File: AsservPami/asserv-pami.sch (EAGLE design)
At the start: 31 parts, among them IC1 NUCLEO-G431KB, IC2 7805TV

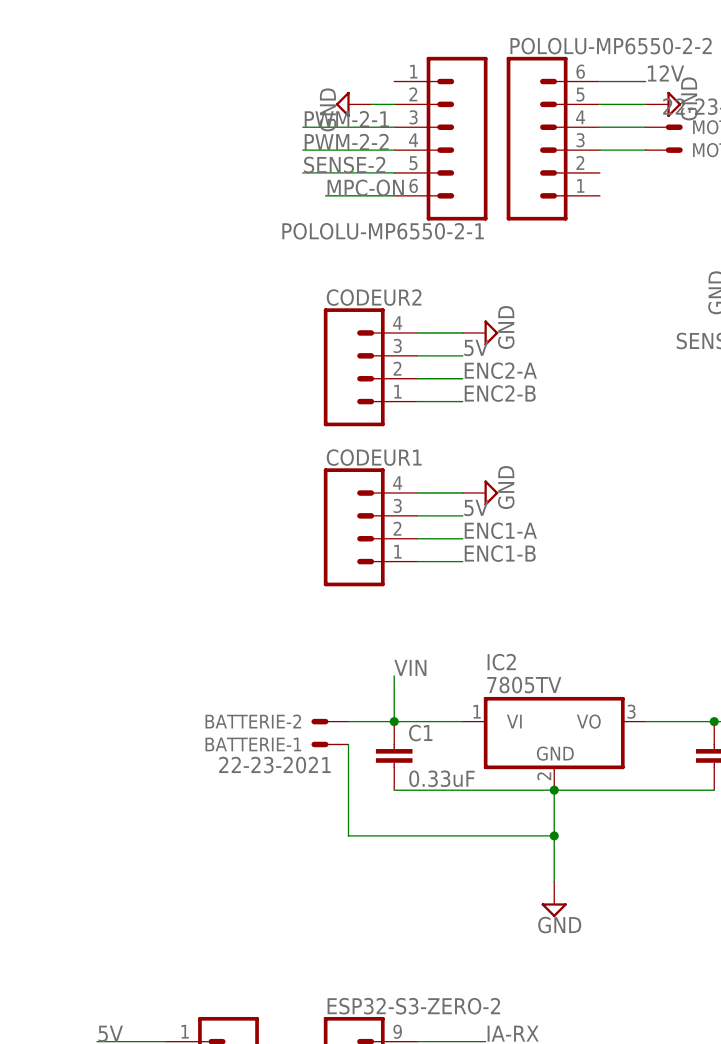
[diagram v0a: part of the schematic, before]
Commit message: ajout BAU et Voltmetre + label
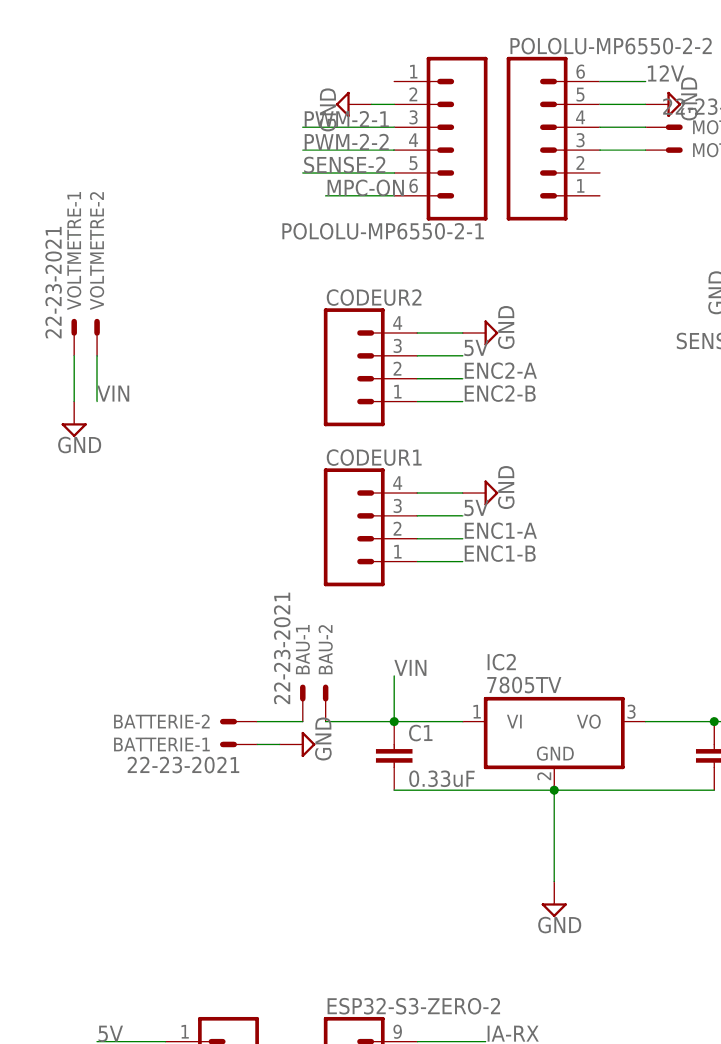
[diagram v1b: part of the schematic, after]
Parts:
- added BAU, VOLTMETRE: 22-23-2021, con-molex:22-23-2021
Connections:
- new net N$7: BATTERIE-2.S, BAU-1.S
- net GND: now also VOLTMETRE-1.S
- net VIN: now also BAU-2.S, VOLTMETRE-2.S; no longer BATTERIE-2.S
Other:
- moved on the sheet: BATTERIE-1, BATTERIE-2
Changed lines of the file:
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@@
 <part name="SUPPLY20" library="supply2" library_urn="urn:adsk.eagle:library:372" deviceset="GND" device=""/>
 <part name="C3" library="capacitor-wima" library_urn="urn:adsk.eagle:library:116" deviceset="C" device="5/2.5" value="0.33uF"/>
+<part name="SUPPLY21" library="supply2" library_urn="urn:adsk.eagle:library:372" deviceset="GND" device=""/>
+<part name="BAU" library="con-molex" library_urn="urn:adsk.eagle:library:165" deviceset="22-23-2021" device=""/>
+<part name="VOLTMETRE" library="con-molex" library_urn="urn:adsk.eagle:library:165" deviceset="22-23-2021" device=""/>
+<part name="SUPPLY22" library="supply2" library_urn="urn:adsk.eagle:library:372" deviceset="GND" device=""/>
 </parts>
 <sheets>
@@
 <attribute name="VALUE" x="63.5" y="120.015" size="1.778" layer="96"/>
 </instance>
-<instance part="BATTERIE" gate="-1" x="45.72" y="114.3" smashed="yes" rot="R180">
-<attribute name="NAME" x="43.18" y="115.062" size="1.524" layer="95" rot="R180"/>
-<attribute name="VALUE" x="46.482" y="112.903" size="1.778" layer="96" rot="R180"/>
-</instance>
-<instance part="BATTERIE" gate="-2" x="45.72" y="116.84" smashed="yes" rot="R180">
-<attribute name="NAME" x="43.18" y="117.602" size="1.524" layer="95" rot="R180"/>
+<instance part="BATTERIE" gate="-1" x="35.56" y="114.3" smashed="yes" rot="R180">
+<attribute name="NAME" x="33.02" y="115.062" size="1.524" layer="95" rot="R180"/>
+<attribute name="VALUE" x="36.322" y="112.903" size="1.778" layer="96" rot="R180"/>
+</instance>
+<instance part="BATTERIE" gate="-2" x="35.56" y="116.84" smashed="yes" rot="R180">
+<attribute name="NAME" x="33.02" y="117.602" size="1.524" layer="95" rot="R180"/>
 </instance>
 <instance part="C1" gate="G$1" x="53.34" y="114.3" smashed="yes">
@@
 <attribute name="NAME" x="126.619" y="105.664" size="1.778" layer="95" rot="R90"/>
 <attribute name="VALUE" x="131.699" y="105.664" size="1.778" layer="96" rot="R90"/>
+</instance>
+<instance part="SUPPLY21" gate="GND" x="43.18" y="114.3" smashed="yes" rot="R90">
+<attribute name="VALUE" x="46.355" y="112.395" size="1.778" layer="96" rot="R90"/>
+</instance>
+<instance part="BAU" gate="-1" x="43.18" y="119.38" smashed="yes" rot="R90">
+<attribute name="NAME" x="43.942" y="121.92" size="1.524" layer="95" rot="R90"/>
+<attribute name="VALUE" x="41.783" y="118.618" size="1.778" layer="96" rot="R90"/>
+</instance>
+<instance part="BAU" gate="-2" x="45.72" y="119.38" smashed="yes" rot="R90">
+<attribute name="NAME" x="46.482" y="121.92" size="1.524" layer="95" rot="R90"/>
+</instance>
+<instance part="VOLTMETRE" gate="-1" x="17.78" y="160.02" smashed="yes" rot="R90">
+<attribute name="NAME" x="18.542" y="162.56" size="1.524" layer="95" rot="R90"/>
+<attribute name="VALUE" x="16.383" y="159.258" size="1.778" layer="96" rot="R90"/>
+</instance>
+<instance part="VOLTMETRE" gate="-2" x="20.32" y="160.02" smashed="yes" rot="R90">
+<attribute name="NAME" x="21.082" y="162.56" size="1.524" layer="95" rot="R90"/>
+</instance>
+<instance part="SUPPLY22" gate="GND" x="17.78" y="149.86" smashed="yes">
+<attribute name="VALUE" x="15.875" y="146.685" size="1.778" layer="96"/>
 </instance>
 </instances>
@@
 <wire x1="71.12" y1="109.22" x2="88.9" y2="109.22" width="0.1524" layer="91"/>
 <junction x="71.12" y="109.22"/>
-<pinref part="BATTERIE" gate="-1" pin="S"/>
-<wire x1="48.26" y1="114.3" x2="48.26" y2="104.14" width="0.1524" layer="91"/>
-<wire x1="48.26" y1="104.14" x2="71.12" y2="104.14" width="0.1524" layer="91"/>
-<wire x1="71.12" y1="104.14" x2="71.12" y2="109.22" width="0.1524" layer="91"/>
-<junction x="71.12" y="104.14"/>
 <pinref part="SUPPLY9" gate="GND" pin="GND"/>
-<wire x1="71.12" y1="104.14" x2="71.12" y2="99.06" width="0.1524" layer="91"/>
+<wire x1="71.12" y1="109.22" x2="71.12" y2="99.06" width="0.1524" layer="91"/>
 </segment>
 <segment>
@@
 <pinref part="SERVO1" gate="J1" pin="3"/>
 </segment>
+<segment>
+<pinref part="SUPPLY21" gate="GND" pin="GND"/>
+<wire x1="38.1" y1="114.3" x2="40.64" y2="114.3" width="0.1524" layer="91"/>
+<pinref part="BATTERIE" gate="-1" pin="S"/>
+</segment>
+<segment>
+<pinref part="SUPPLY22" gate="GND" pin="GND"/>
+<wire x1="17.78" y1="157.48" x2="17.78" y2="152.4" width="0.1524" layer="91"/>
+<pinref part="VOLTMETRE" gate="-1" pin="S"/>
+</segment>
 </net>
 <net name="N$1" class="0">
@@
 <net name="VIN" class="0">
 <segment>
-<pinref part="BATTERIE" gate="-2" pin="S"/>
 <pinref part="C1" gate="G$1" pin="1"/>
-<wire x1="48.26" y1="116.84" x2="53.34" y2="116.84" width="0.1524" layer="91"/>
 <pinref part="IC2" gate="A1" pin="VI"/>
 <wire x1="53.34" y1="116.84" x2="60.96" y2="116.84" width="0.1524" layer="91"/>
@@
 <wire x1="53.34" y1="116.84" x2="53.34" y2="121.92" width="0.1524" layer="91"/>
 <label x="53.34" y="121.92" size="1.778" layer="95"/>
+<pinref part="BAU" gate="-2" pin="S"/>
+<wire x1="45.72" y1="116.84" x2="53.34" y2="116.84" width="0.1524" layer="91"/>
 </segment>
 <segment>
@@
 <label x="132.08" y="101.6" size="1.778" layer="95"/>
 </segment>
+<segment>
+<pinref part="VOLTMETRE" gate="-2" pin="S"/>
+<wire x1="20.32" y1="157.48" x2="20.32" y2="152.4" width="0.1524" layer="91"/>
+<label x="20.32" y="152.4" size="1.778" layer="95"/>
+</segment>
 </net>
 <net name="SDA" class="0">
@@
 </segment>
 </net>
+<net name="N$7" class="0">
+<segment>
+<pinref part="BATTERIE" gate="-2" pin="S"/>
+<pinref part="BAU" gate="-1" pin="S"/>
+<wire x1="38.1" y1="116.84" x2="43.18" y2="116.84" width="0.1524" layer="91"/>
+</segment>
+</net>

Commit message: fix i2c
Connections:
- net SCL: now also ESP32-S3-ZERO-2.2; no longer ESP32-S3-ZERO-2.6
- net SDA: now also ESP32-S3-ZERO-2.3; no longer ESP32-S3-ZERO-2.7
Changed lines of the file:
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@@
 <net name="SDA" class="0">
-<segment>
-<pinref part="ESP32-S3-ZERO-2" gate="J1" pin="7"/>
-<wire x1="55.88" y1="76.2" x2="63.5" y2="76.2" width="0.1524" layer="91"/>
-<label x="63.5" y="76.2" size="1.778" layer="95"/>
-</segment>
 <segment>
 <pinref part="I2C" gate="J1" pin="1"/>
@@
 <label x="96.52" y="68.58" size="1.778" layer="95" rot="R90"/>
 </segment>
+<segment>
+<wire x1="55.88" y1="66.04" x2="63.5" y2="66.04" width="0.1524" layer="91"/>
+<label x="63.5" y="66.04" size="1.778" layer="95"/>
+<pinref part="ESP32-S3-ZERO-2" gate="J1" pin="3"/>
+</segment>
 </net>
 <net name="SCL" class="0">
-<segment>
-<pinref part="ESP32-S3-ZERO-2" gate="J1" pin="6"/>
-<wire x1="55.88" y1="73.66" x2="63.5" y2="73.66" width="0.1524" layer="91"/>
-<label x="63.5" y="73.66" size="1.778" layer="95"/>
-</segment>
 <segment>
 <pinref part="I2C" gate="J1" pin="2"/>
@@
 <label x="99.06" y="68.58" size="1.778" layer="95" rot="R90"/>
 </segment>
+<segment>
+<wire x1="55.88" y1="63.5" x2="63.5" y2="63.5" width="0.1524" layer="91"/>
+<label x="63.5" y="63.5" size="1.778" layer="95"/>
+<pinref part="ESP32-S3-ZERO-2" gate="J1" pin="2"/>
+</segment>
 </net>

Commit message: fix name
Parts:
- renumbered ESP32-S3-ZERO-1 to ESP32-C3-ZERO-1, ESP32-S3-ZERO-2 to ESP32-C3-ZERO-2
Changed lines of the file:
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@@
 <part name="POLOLU-U3V40F12" library="SparkFun-Connectors" library_urn="urn:adsk.eagle:library:513" deviceset="CONN_06" device="NO_SILK_FEMALE_PTH" package3d_urn="urn:adsk.eagle:package:38130/2"/>
 <part name="SUPPLY10" library="supply2" library_urn="urn:adsk.eagle:library:372" deviceset="GND" device=""/>
-<part name="ESP32-S3-ZERO-2" library="SparkFun-Connectors" library_urn="urn:adsk.eagle:library:513" deviceset="CONN_09" device="LONGPADS" package3d_urn="urn:adsk.eagle:package:38155/2"/>
-<part name="ESP32-S3-ZERO-1" library="SparkFun-Connectors" library_urn="urn:adsk.eagle:library:513" deviceset="CONN_09" device="LONGPADS" package3d_urn="urn:adsk.eagle:package:38155/2"/>
+<part name="ESP32-C3-ZERO-2" library="SparkFun-Connectors" library_urn="urn:adsk.eagle:library:513" deviceset="CONN_09" device="LONGPADS" package3d_urn="urn:adsk.eagle:package:38155/2"/>
+<part name="ESP32-C3-ZERO-1" library="SparkFun-Connectors" library_urn="urn:adsk.eagle:library:513" deviceset="CONN_09" device="LONGPADS" package3d_urn="urn:adsk.eagle:package:38155/2"/>
 <part name="SUPPLY13" library="supply2" library_urn="urn:adsk.eagle:library:372" deviceset="GND" device=""/>
 <part name="I2C" library="SparkFun-Connectors" library_urn="urn:adsk.eagle:library:513" deviceset="CONN_04" device="PTH" package3d_urn="urn:adsk.eagle:package:38085/2"/>
@@
 <attribute name="VALUE" x="122.555" y="98.425" size="1.778" layer="96"/>
 </instance>
-<instance part="ESP32-S3-ZERO-2" gate="J1" x="45.72" y="71.12" smashed="yes">
+<instance part="ESP32-C3-ZERO-2" gate="J1" x="45.72" y="71.12" smashed="yes">
 <attribute name="VALUE" x="45.72" y="56.134" size="1.778" layer="96" font="vector"/>
 <attribute name="NAME" x="45.72" y="84.328" size="1.778" layer="95" font="vector"/>
 </instance>
-<instance part="ESP32-S3-ZERO-1" gate="J1" x="38.1" y="71.12" smashed="yes" rot="R180">
+<instance part="ESP32-C3-ZERO-1" gate="J1" x="38.1" y="71.12" smashed="yes" rot="R180">
 <attribute name="VALUE" x="38.1" y="86.106" size="1.778" layer="96" font="vector" rot="R180"/>
 <attribute name="NAME" x="38.1" y="57.912" size="1.778" layer="95" font="vector" rot="R180"/>
@@
 </segment>
 <segment>
-<pinref part="ESP32-S3-ZERO-1" gate="J1" pin="2"/>
+<pinref part="ESP32-C3-ZERO-1" gate="J1" pin="2"/>
 <pinref part="SUPPLY13" gate="GND" pin="GND"/>
 <wire x1="27.94" y1="78.74" x2="20.32" y2="78.74" width="0.1524" layer="91"/>
@@
 </segment>
 <segment>
-<pinref part="ESP32-S3-ZERO-2" gate="J1" pin="8"/>
+<pinref part="ESP32-C3-ZERO-2" gate="J1" pin="8"/>
 <wire x1="55.88" y1="78.74" x2="63.5" y2="78.74" width="0.1524" layer="91"/>
 <label x="63.5" y="78.74" size="1.778" layer="95"/>
@@
 </segment>
 <segment>
-<pinref part="ESP32-S3-ZERO-2" gate="J1" pin="9"/>
+<pinref part="ESP32-C3-ZERO-2" gate="J1" pin="9"/>
 <wire x1="55.88" y1="81.28" x2="63.5" y2="81.28" width="0.1524" layer="91"/>
 <label x="63.5" y="81.28" size="1.778" layer="95"/>
@@
 </segment>
 <segment>
-<pinref part="ESP32-S3-ZERO-1" gate="J1" pin="1"/>
+<pinref part="ESP32-C3-ZERO-1" gate="J1" pin="1"/>
 <wire x1="27.94" y1="81.28" x2="20.32" y2="81.28" width="0.1524" layer="91"/>
 <label x="20.32" y="81.28" size="1.778" layer="95"/>
@@
 <wire x1="55.88" y1="66.04" x2="63.5" y2="66.04" width="0.1524" layer="91"/>
 <label x="63.5" y="66.04" size="1.778" layer="95"/>
-<pinref part="ESP32-S3-ZERO-2" gate="J1" pin="3"/>
+<pinref part="ESP32-C3-ZERO-2" gate="J1" pin="3"/>
 </segment>
 </net>
@@
 <wire x1="55.88" y1="63.5" x2="63.5" y2="63.5" width="0.1524" layer="91"/>
 <label x="63.5" y="63.5" size="1.778" layer="95"/>
-<pinref part="ESP32-S3-ZERO-2" gate="J1" pin="2"/>
+<pinref part="ESP32-C3-ZERO-2" gate="J1" pin="2"/>
 </segment>
 </net>
@@
 <wire x1="27.94" y1="73.66" x2="17.78" y2="73.66" width="0.1524" layer="91"/>
 <label x="17.78" y="73.66" size="1.778" layer="95"/>
-<pinref part="ESP32-S3-ZERO-1" gate="J1" pin="4"/>
+<pinref part="ESP32-C3-ZERO-1" gate="J1" pin="4"/>
 </segment>
 </net>
@@
 <wire x1="27.94" y1="71.12" x2="17.78" y2="71.12" width="0.1524" layer="91"/>
 <label x="17.78" y="71.12" size="1.778" layer="95"/>
-<pinref part="ESP32-S3-ZERO-1" gate="J1" pin="5"/>
+<pinref part="ESP32-C3-ZERO-1" gate="J1" pin="5"/>
 </segment>
 </net>
@@
 <wire x1="27.94" y1="68.58" x2="17.78" y2="68.58" width="0.1524" layer="91"/>
 <label x="17.78" y="68.58" size="1.778" layer="95"/>
-<pinref part="ESP32-S3-ZERO-1" gate="J1" pin="6"/>
+<pinref part="ESP32-C3-ZERO-1" gate="J1" pin="6"/>
 </segment>
 </net>
@@
 <wire x1="27.94" y1="66.04" x2="17.78" y2="66.04" width="0.1524" layer="91"/>
 <label x="17.78" y="66.04" size="1.778" layer="95"/>
-<pinref part="ESP32-S3-ZERO-1" gate="J1" pin="7"/>
+<pinref part="ESP32-C3-ZERO-1" gate="J1" pin="7"/>
 </segment>
 </net>
@@
 <wire x1="27.94" y1="63.5" x2="17.78" y2="63.5" width="0.1524" layer="91"/>
 <label x="17.78" y="63.5" size="1.778" layer="95"/>
-<pinref part="ESP32-S3-ZERO-1" gate="J1" pin="8"/>
+<pinref part="ESP32-C3-ZERO-1" gate="J1" pin="8"/>
 </segment>
 </net>
@@
 <wire x1="27.94" y1="60.96" x2="17.78" y2="60.96" width="0.1524" layer="91"/>
 <label x="17.78" y="60.96" size="1.778" layer="95"/>
-<pinref part="ESP32-S3-ZERO-1" gate="J1" pin="9"/>
+<pinref part="ESP32-C3-ZERO-1" gate="J1" pin="9"/>
 </segment>
 </net>
@@
 <pinref part="UART" gate="-1" pin="S"/>
 <wire x1="68.58" y1="66.04" x2="68.58" y2="68.58" width="0.1524" layer="91"/>
-<pinref part="ESP32-S3-ZERO-2" gate="J1" pin="4"/>
+<pinref part="ESP32-C3-ZERO-2" gate="J1" pin="4"/>
 <wire x1="68.58" y1="68.58" x2="55.88" y2="68.58" width="0.1524" layer="91"/>
 </segment>
@@
 <pinref part="UART" gate="-2" pin="S"/>
 <wire x1="66.04" y1="66.04" x2="66.04" y2="71.12" width="0.1524" layer="91"/>
-<pinref part="ESP32-S3-ZERO-2" gate="J1" pin="5"/>
+<pinref part="ESP32-C3-ZERO-2" gate="J1" pin="5"/>
 <wire x1="66.04" y1="71.12" x2="55.88" y2="71.12" width="0.1524" layer="91"/>
 </segment>

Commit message: fix pami woard
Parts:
- added R-5K5, R-5K6: (no value), rcl:R-EU_0204/7
- C1: value 0.33uF -> 0.1uF
- C2: value 0.1uF -> 22uF
- C3: value 0.33uF -> 33uF
- IC2: value 7805TV -> L4941BV
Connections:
- net 5V: now also R-5K5.2, R-5K6.2; no longer IC1.+5V
- net SCL: now also R-5K6.1
- net SDA: now also R-5K5.1
- net VIN: now also IC1.VIN
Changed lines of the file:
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@@
 <part name="USB-DEBUG" library="SparkFun-Connectors" library_urn="urn:adsk.eagle:library:513" deviceset="CONN_05" device="NO_SILK" package3d_urn="urn:adsk.eagle:package:38108/2"/>
 <part name="SUPPLY8" library="supply2" library_urn="urn:adsk.eagle:library:372" deviceset="GND" device=""/>
-<part name="IC2" library="linear" library_urn="urn:adsk.eagle:library:262" deviceset="78*" device="TV" technology="05"/>
+<part name="IC2" library="linear" library_urn="urn:adsk.eagle:library:262" deviceset="78*" device="TV" technology="05" value="L4941BV"/>
 <part name="BATTERIE" library="con-molex" library_urn="urn:adsk.eagle:library:165" deviceset="22-23-2021" device=""/>
-<part name="C1" library="capacitor-wima" library_urn="urn:adsk.eagle:library:116" deviceset="C" device="5/2.5" value="0.33uF"/>
-<part name="C2" library="capacitor-wima" library_urn="urn:adsk.eagle:library:116" deviceset="C" device="5/2.5" value="0.1uF"/>
+<part name="C1" library="capacitor-wima" library_urn="urn:adsk.eagle:library:116" deviceset="C" device="5/2.5" value="0.1uF"/>
+<part name="C2" library="capacitor-wima" library_urn="urn:adsk.eagle:library:116" deviceset="C" device="5/2.5" value="22uF"/>
 <part name="SUPPLY9" library="supply2" library_urn="urn:adsk.eagle:library:372" deviceset="GND" device=""/>
 <part name="FRAME1" library="frames" library_urn="urn:adsk.eagle:library:229" deviceset="A4-SMALL-DOCFIELD" device=""/>
@@
 <part name="SUPPLY19" library="supply2" library_urn="urn:adsk.eagle:library:372" deviceset="GND" device=""/>
 <part name="SUPPLY20" library="supply2" library_urn="urn:adsk.eagle:library:372" deviceset="GND" device=""/>
-<part name="C3" library="capacitor-wima" library_urn="urn:adsk.eagle:library:116" deviceset="C" device="5/2.5" value="0.33uF"/>
+<part name="C3" library="capacitor-wima" library_urn="urn:adsk.eagle:library:116" deviceset="C" device="5/2.5" value="33uF"/>
 <part name="SUPPLY21" library="supply2" library_urn="urn:adsk.eagle:library:372" deviceset="GND" device=""/>
 <part name="BAU" library="con-molex" library_urn="urn:adsk.eagle:library:165" deviceset="22-23-2021" device=""/>
 <part name="VOLTMETRE" library="con-molex" library_urn="urn:adsk.eagle:library:165" deviceset="22-23-2021" device=""/>
 <part name="SUPPLY22" library="supply2" library_urn="urn:adsk.eagle:library:372" deviceset="GND" device=""/>
+<part name="R-5K5" library="rcl" library_urn="urn:adsk.eagle:library:334" deviceset="R-EU_" device="0204/7" package3d_urn="urn:adsk.eagle:package:23498/1"/>
+<part name="R-5K6" library="rcl" library_urn="urn:adsk.eagle:library:334" deviceset="R-EU_" device="0204/7" package3d_urn="urn:adsk.eagle:package:23498/1"/>
 </parts>
 <sheets>
@@
 <attribute name="VALUE" x="15.875" y="146.685" size="1.778" layer="96"/>
 </instance>
+<instance part="R-5K5" gate="G$1" x="48.26" y="35.56" smashed="yes" rot="R270">
+<attribute name="NAME" x="49.7586" y="39.37" size="1.778" layer="95" rot="R270"/>
+<attribute name="VALUE" x="44.958" y="39.37" size="1.778" layer="96" rot="R270"/>
+</instance>
+<instance part="R-5K6" gate="G$1" x="53.34" y="35.56" smashed="yes" rot="R270">
+<attribute name="NAME" x="54.8386" y="39.37" size="1.778" layer="95" rot="R270"/>
+<attribute name="VALUE" x="50.038" y="39.37" size="1.778" layer="96" rot="R270"/>
+</instance>
 </instances>
 <busses>
@@
 <net name="5V" class="0">
 <segment>
-<pinref part="IC1" gate="G$1" pin="+5V"/>
-<wire x1="144.78" y1="165.1" x2="149.86" y2="165.1" width="0.1524" layer="91"/>
-<label x="149.86" y="165.1" size="1.778" layer="95"/>
-</segment>
-<segment>
 <pinref part="CODEUR2" gate="J1" pin="3"/>
 <wire x1="55.88" y1="157.48" x2="60.96" y2="157.48" width="0.1524" layer="91"/>
@@
 <label x="81.28" y="40.64" size="1.778" layer="95" rot="R270"/>
 <pinref part="SERVO1" gate="J1" pin="2"/>
+</segment>
+<segment>
+<pinref part="R-5K5" gate="G$1" pin="2"/>
+<wire x1="48.26" y1="30.48" x2="48.26" y2="22.86" width="0.1524" layer="91"/>
+<label x="48.26" y="22.86" size="1.778" layer="95" rot="R90"/>
+</segment>
+<segment>
+<pinref part="R-5K6" gate="G$1" pin="2"/>
+<wire x1="53.34" y1="30.48" x2="53.34" y2="22.86" width="0.1524" layer="91"/>
+<label x="53.34" y="22.86" size="1.778" layer="95" rot="R90"/>
 </segment>
 </net>
@@
 <label x="20.32" y="152.4" size="1.778" layer="95"/>
 </segment>
+<segment>
+<pinref part="IC1" gate="G$1" pin="VIN"/>
+<wire x1="144.78" y1="172.72" x2="149.86" y2="172.72" width="0.1524" layer="91"/>
+<label x="149.86" y="172.72" size="1.778" layer="95"/>
+</segment>
 </net>
 <net name="SDA" class="0">
@@
 <pinref part="ESP32-C3-ZERO-2" gate="J1" pin="3"/>
 </segment>
+<segment>
+<pinref part="R-5K5" gate="G$1" pin="1"/>
+<wire x1="48.26" y1="40.64" x2="48.26" y2="45.72" width="0.1524" layer="91"/>
+<label x="48.26" y="45.72" size="1.778" layer="95"/>
+</segment>
 </net>
 <net name="SCL" class="0">
@@
 <label x="63.5" y="63.5" size="1.778" layer="95"/>
 <pinref part="ESP32-C3-ZERO-2" gate="J1" pin="2"/>
+</segment>
+<segment>
+<pinref part="R-5K6" gate="G$1" pin="1"/>
+<wire x1="53.34" y1="40.64" x2="53.34" y2="45.72" width="0.1524" layer="91"/>
+<label x="53.34" y="45.72" size="1.778" layer="95"/>
 </segment>
 </net>
@@
 </sheet>
 </sheets>
+<errors>
+</errors>
 </schematic>
 </drawing>
